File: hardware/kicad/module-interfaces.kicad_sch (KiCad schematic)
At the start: 24 parts, among them J20 socket20, J21 socket20, J30 header20, J31 header20

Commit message: Clean KiCad 9 root-hierarchy ERC in the generator; add outline DRC to kicad_check
- make_design.py: place symbols, wires, labels and no-connects on the 1.27 mm grid
  (endpoint_off_grid 872 -> 0); add PWR_FLAG on +5V_FUSED and GND, which are fed
  only from off-board USB through passive Pico socket contacts and fuse F1
  (power_pin_not_driven 2 -> 0); generate 74HC4067 Y/Z as passive analog-switch
  terminals instead of bidirectional.
- kicad_check.py: every remaining ERC item needs a reason, endpoint_off_grid and
  lib_symbol_* must be 0, outline-board DRC error count recorded and gated.
- validate.py: exclude '#' power/flag symbols from the physical instance inventory.

Refs #11

Co-Authored-By: Claude Opus 5.5 <noreply@anthropic.com>
Claude-Session: https://claude.ai/code/session_018oLpisCWqu84U1dDpzLDZ4
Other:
- moved on the sheet: J20, J21, J30, J31, R60, R61, R62, R63, R64, R65, R66, R67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

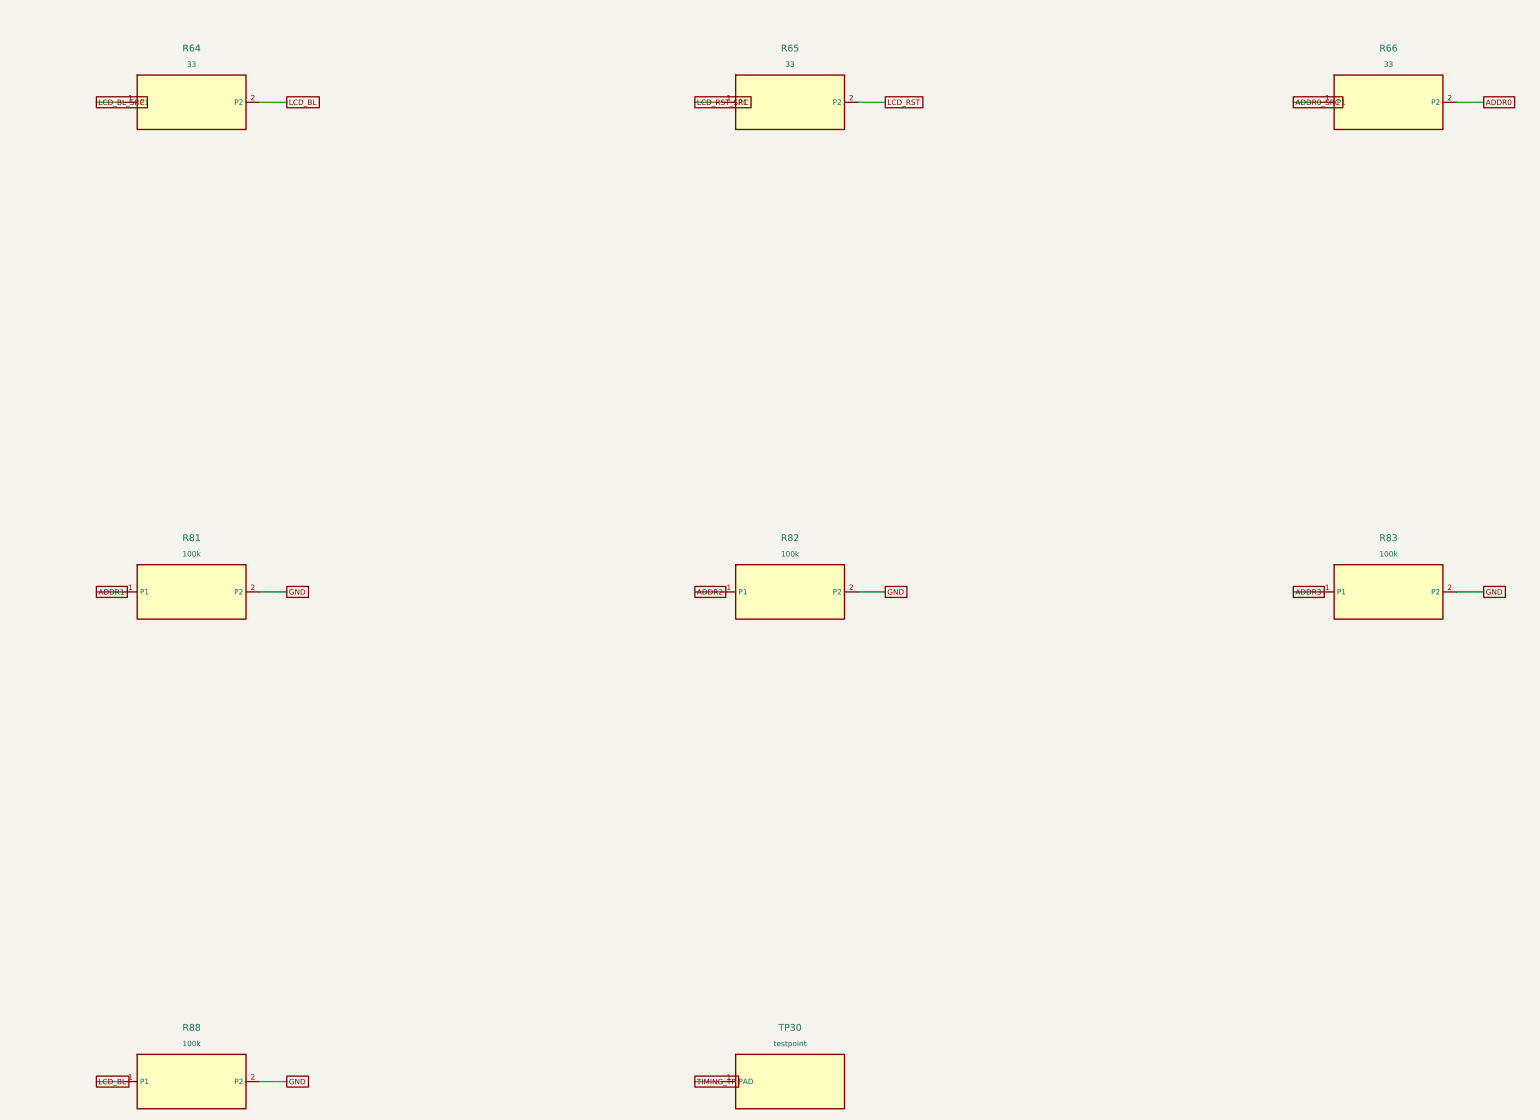
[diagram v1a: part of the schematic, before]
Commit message: Replace the GP13-LCD_BL tie with an open-drain MOSFET backlight stage (#41)
Module R16 (10k) pulls LCD_BL / CAT1 EN to VSYS (~5 V), so the old carrier
wiring (GP13 -> R64 -> LCD_BL, R88 100k to GND) put an undriven GP13 near
4.5 V, above the RP2040 IOVDD + 0.5 V absolute maximum. Neither removing R88
nor accepting an undocumented clamp current meets the pin limits (#19).

Circuit (scripts/make_design.py + catalog/components.json, regenerated
sheets/netlist/BOM/connections/circuit.json):
- new generic record `nmos-ll` (logic-level N-channel MOSFET; no MPN, no
  LCSC code, footprint unassigned, exact part at G08)
- R64 now feeds net LCD_BL_GATE -> Q1 gate; R88 is the gate pull-down;
  Q1 drain = LCD_BL (J30 pos 17, header nets unchanged), source = GND
- pending_g01_changes[g01-r88-backlight-default] ->
  DESIGN_APPLIED_BENCH_CHECK_PENDING

Result: the GP13 pad sees only its own drive or 0 V in every state
(USB 4.75-5.25 V, reset, BOOTSEL, both power-up orders, normal operation);
backlight default ON, GP13 high = OFF.

Firmware: inverted polarity via LCD_BL_LEVEL_OFF/ON in lcd_safe_pins.h;
the early hook drives GP13 high (dark), scope_display_backlight() drives it
low to light the panel. SCOPE_ENABLE_LCD stays default OFF.

Evidence/docs: design/evidence/backlight-interface.md (per-state
voltage/current table, alternatives weighed, bench items),
module-power.json backlight-regulator-en-thresholds (unknown),
power-contract.json backlight_default/gp13_pad_voltage per power state,
narrative power page, release-gates G01/G06 notes, LOCAL-HANDOFF G01/G06,
LCD-BACKEND.md, acceptance row BACKLIGHT_GP13_INTERFACE (NOT_RUN).

Validation: validate_extra._gp13_backlight_interface asserts GP13's net has
no resistive DC path below 1 MOhm to +5V_FUSED/VBUS_USB/LCD_BL, the
gate/LCD_BL net membership, the frozen J30/J31 map, the firmware OFF level
and that G01/G06 stay OPEN.

Co-Authored-By: Claude Fable 5.1 <noreply@anthropic.com>
Claude-Session: https://claude.ai/code/session_01LdS1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
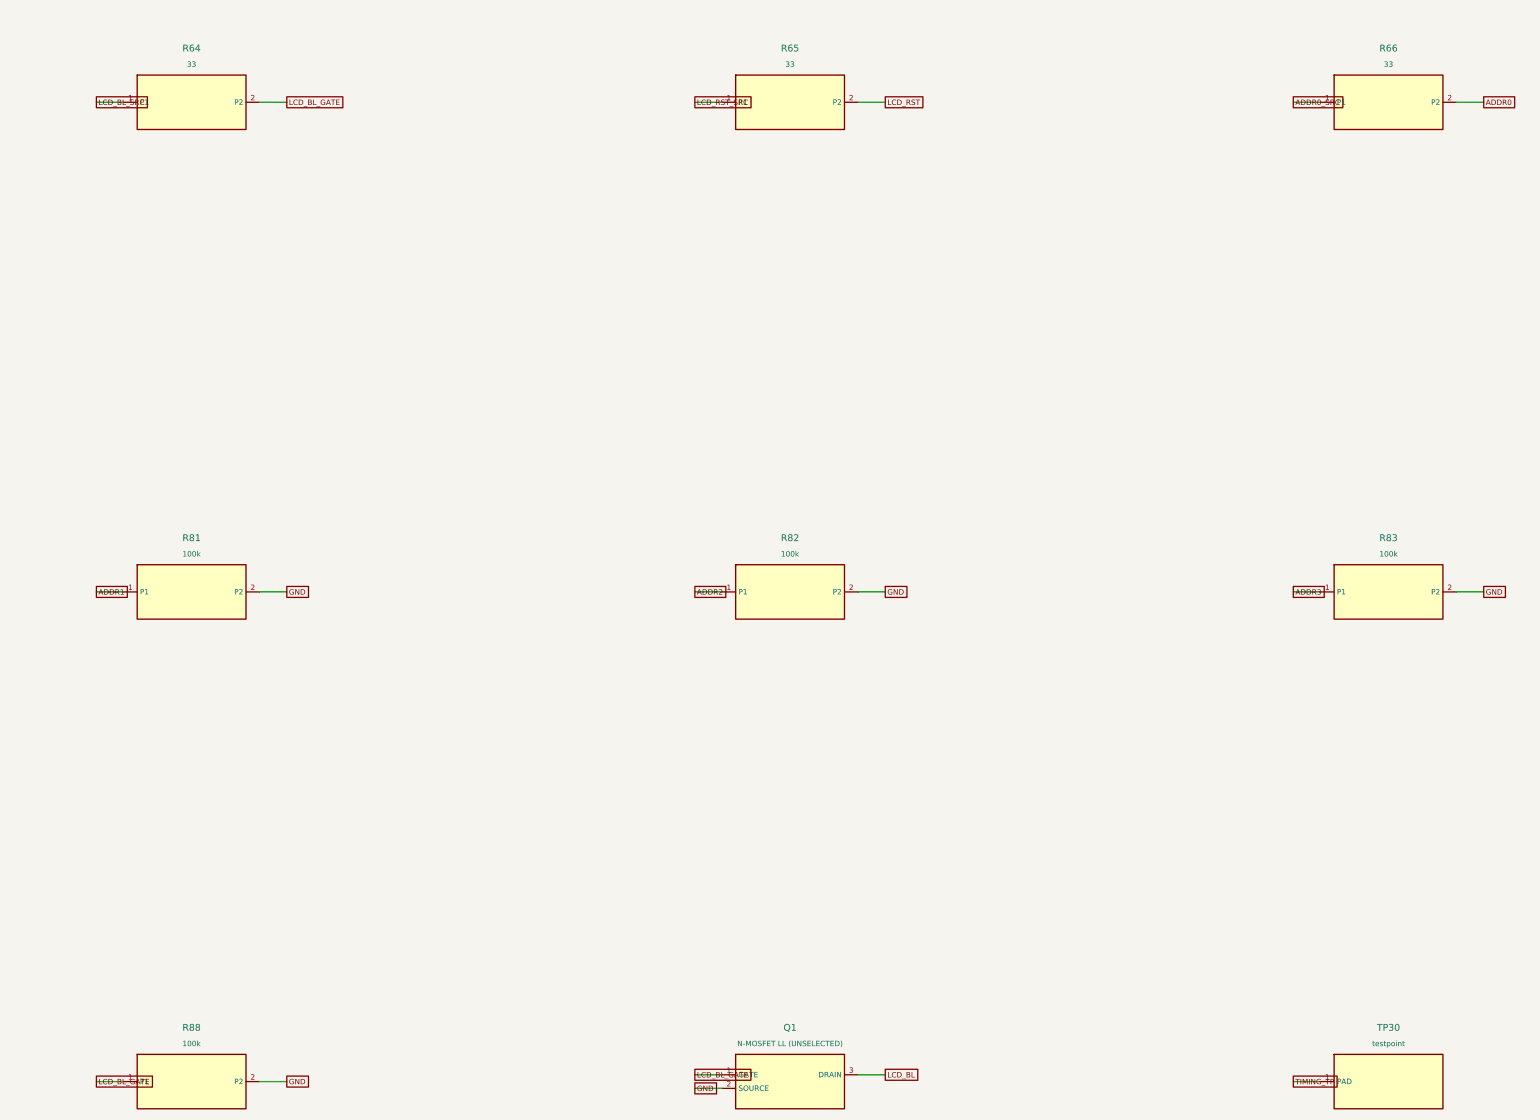
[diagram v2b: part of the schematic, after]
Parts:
- added Q1: N-MOSFET LL (UNSELECTED), symbol ZudoScope10:nmos-ll
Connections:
- net GND: now also Q1.2 (SOURCE)
- net LCD_BL: now also Q1.3 (DRAIN); no longer R64.2 (P2), R88.1 (P1)
- new net LCD_BL_GATE: Q1.1 (GATE), R64.2 (P2), R88.1 (P1)
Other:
- moved on the sheet: TP30
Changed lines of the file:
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@@
 (global_label "LCD_BL_SRC" (shape passive) (at 138.43 146.05 0) (effects (font (size 1.0 1.0)) (justify left)) (property "Intersheetrefs" "${INTERSHEET_REFS}" (at 138.43 146.05 0) (effects (font (size 1 1)) hide)))
 (wire (pts (xy 168.91 146.05) (xy 173.99 146.05)) (stroke (width 0) (type default)))
-(global_label "LCD_BL" (shape passive) (at 173.99 146.05 180) (effects (font (size 1.0 1.0)) (justify left)) (property "Intersheetrefs" "${INTERSHEET_REFS}" (at 173.99 146.05 180) (effects (font (size 1 1)) hide)))
+(global_label "LCD_BL_GATE" (shape passive) (at 173.99 146.05 180) (effects (font (size 1.0 1.0)) (justify left)) (property "Intersheetrefs" "${INTERSHEET_REFS}" (at 173.99 146.05 180) (effects (font (size 1 1)) hide)))
 (symbol (lib_id "ZudoScope10:r33") (at 267.97 146.05 0) (unit 1) (in_bom yes) (on_board yes) (dnp no)
 (property "Reference" "R65" (at 267.97 135.97 0) (effects (font (size 1.27 1.27))))
@@
 (instances (project "zudo-scope10-p0" (path "/566b858e-08cf-50b5-8b4f-1a68e92bd689/f8eca76a-766f-52ab-8ac6-f65d72b3995e" (reference "R88") (unit 1)))))
 (wire (pts (xy 143.51 328.93) (xy 138.43 328.93)) (stroke (width 0) (type default)))
-(global_label "LCD_BL" (shape passive) (at 138.43 328.93 0) (effects (font (size 1.0 1.0)) (justify left)) (property "Intersheetrefs" "${INTERSHEET_REFS}" (at 138.43 328.93 0) (effects (font (size 1 1)) hide)))
+(global_label "LCD_BL_GATE" (shape passive) (at 138.43 328.93 0) (effects (font (size 1.0 1.0)) (justify left)) (property "Intersheetrefs" "${INTERSHEET_REFS}" (at 138.43 328.93 0) (effects (font (size 1 1)) hide)))
 (wire (pts (xy 168.91 328.93) (xy 173.99 328.93)) (stroke (width 0) (type default)))
 (global_label "GND" (shape passive) (at 173.99 328.93 180) (effects (font (size 1.0 1.0)) (justify left)) (property "Intersheetrefs" "${INTERSHEET_REFS}" (at 173.99 328.93 180) (effects (font (size 1 1)) hide)))
-(symbol (lib_id "ZudoScope10:testpoint") (at 267.97 328.93 0) (unit 1) (in_bom yes) (on_board yes) (dnp no)
-(property "Reference" "TP30" (at 267.97 318.85 0) (effects (font (size 1.27 1.27))))
-(property "Value" "testpoint" (at 267.97 321.85 0) (effects (font (size 1.0 1.0))))
-(property "Footprint" "TestPoint:TestPoint_Pad_D1.0mm" (at 267.97 328.93 0) (effects (font (size 1.0 1.0)) hide))
+(symbol (lib_id "ZudoScope10:nmos-ll") (at 267.97 328.93 0) (unit 1) (in_bom yes) (on_board yes) (dnp no)
+(property "Reference" "Q1" (at 267.97 318.85 0) (effects (font (size 1.27 1.27))))
+(property "Value" "N-MOSFET LL (UNSELECTED)" (at 267.97 321.85 0) (effects (font (size 1.0 1.0))))
+(property "Footprint" "" (at 267.97 328.93 0) (effects (font (size 1.0 1.0)) hide))
 (property "Datasheet" "" (at 267.97 328.93 0) (effects (font (size 1.0 1.0)) hide))
-(property "Record" "testpoint" (at 267.97 328.93 0) (effects (font (size 1.0 1.0)) hide))
+(property "Record" "nmos-ll" (at 267.97 328.93 0) (effects (font (size 1.0 1.0)) hide))
+(pin "1")
+(pin "2")
+(pin "3")
+(instances (project "zudo-scope10-p0" (path "/566b858e-08cf-50b5-8b4f-1a68e92bd689/f8eca76a-766f-52ab-8ac6-f65d72b3995e" (reference "Q1") (unit 1)))))
+(wire (pts (xy 255.27 327.66) (xy 250.19 327.66)) (stroke (width 0) (type default)))
+(global_label "LCD_BL_GATE" (shape passive) (at 250.19 327.66 0) (effects (font (size 1.0 1.0)) (justify left)) (property "Intersheetrefs" "${INTERSHEET_REFS}" (at 250.19 327.66 0) (effects (font (size 1 1)) hide)))
+(wire (pts (xy 255.27 330.2) (xy 250.19 330.2)) (stroke (width 0) (type default)))
+(global_label "GND" (shape passive) (at 250.19 330.2 0) (effects (font (size 1.0 1.0)) (justify left)) (property "Intersheetrefs" "${INTERSHEET_REFS}" (at 250.19 330.2 0) (effects (font (size 1 1)) hide)))
+(wire (pts (xy 280.67 327.66) (xy 285.75 327.66)) (stroke (width 0) (type default)))
+(global_label "LCD_BL" (shape passive) (at 285.75 327.66 180) (effects (font (size 1.0 1.0)) (justify left)) (property "Intersheetrefs" "${INTERSHEET_REFS}" (at 285.75 327.66 180) (effects (font (size 1 1)) hide)))
+(symbol (lib_id "ZudoScope10:testpoint") (at 379.73 328.93 0) (unit 1) (in_bom yes) (on_board yes) (dnp no)
+(property "Reference" "TP30" (at 379.73 318.85 0) (effects (font (size 1.27 1.27))))
+(property "Value" "testpoint" (at 379.73 321.85 0) (effects (font (size 1.0 1.0))))
+(property "Footprint" "TestPoint:TestPoint_Pad_D1.0mm" (at 379.73 328.93 0) (effects (font (size 1.0 1.0)) hide))
+(property "Datasheet" "" (at 379.73 328.93 0) (effects (font (size 1.0 1.0)) hide))
+(property "Record" "testpoint" (at 379.73 328.93 0) (effects (font (size 1.0 1.0)) hide))
 (pin "1")
 (instances (project "zudo-scope10-p0" (path "/566b858e-08cf-50b5-8b4f-1a68e92bd689/f8eca76a-766f-52ab-8ac6-f65d72b3995e" (reference "TP30") (unit 1)))))
-(wire (pts (xy 255.27 328.93) (xy 250.19 328.93)) (stroke (width 0) (type default)))
-(global_label "TIMING_TP" (shape passive) (at 250.19 328.93 0) (effects (font (size 1.0 1.0)) (justify left)) (property "Intersheetrefs" "${INTERSHEET_REFS}" (at 250.19 328.93 0) (effects (font (size 1 1)) hide)))
+(wire (pts (xy 367.03 328.93) (xy 361.95 328.93)) (stroke (width 0) (type default)))
+(global_label "TIMING_TP" (shape passive) (at 361.95 328.93 0) (effects (font (size 1.0 1.0)) (justify left)) (property "Intersheetrefs" "${INTERSHEET_REFS}" (at 361.95 328.93 0) (effects (font (size 1 1)) hide)))
 )
